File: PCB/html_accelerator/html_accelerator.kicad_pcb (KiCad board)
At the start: 4 copper layers, 129.3 x 104.4 mm, 170 parts, among them J1 Bus_PCI_Express_x16, J2 PCIexpress_bracket, U1 MCS9990, U10 AU6438BS, U11 EMMC_4G, U12 MCS9990, U2 AP1513, U3 CAT24C256YI-GT3, U4 AU6438BS, U5 EMMC_4G, U6 EMMC_4G, U7 EMMC_4G, U8 AU6438BS, U9 AU6438BS, Y1 12MHz, Y2 12MHz, Y3 12MHz, Y4 12MHz, Y5 12MHz

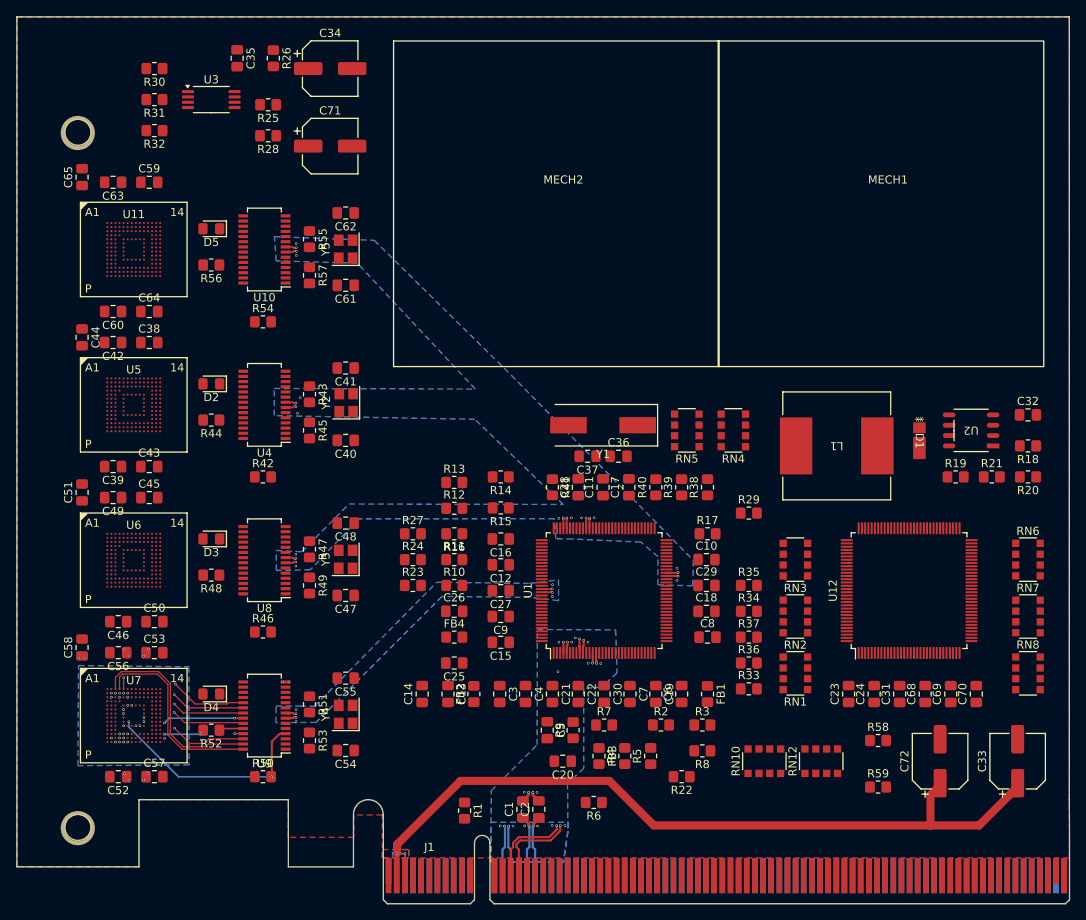
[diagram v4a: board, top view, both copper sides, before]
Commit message: highspeed routing + EMMC routing #1
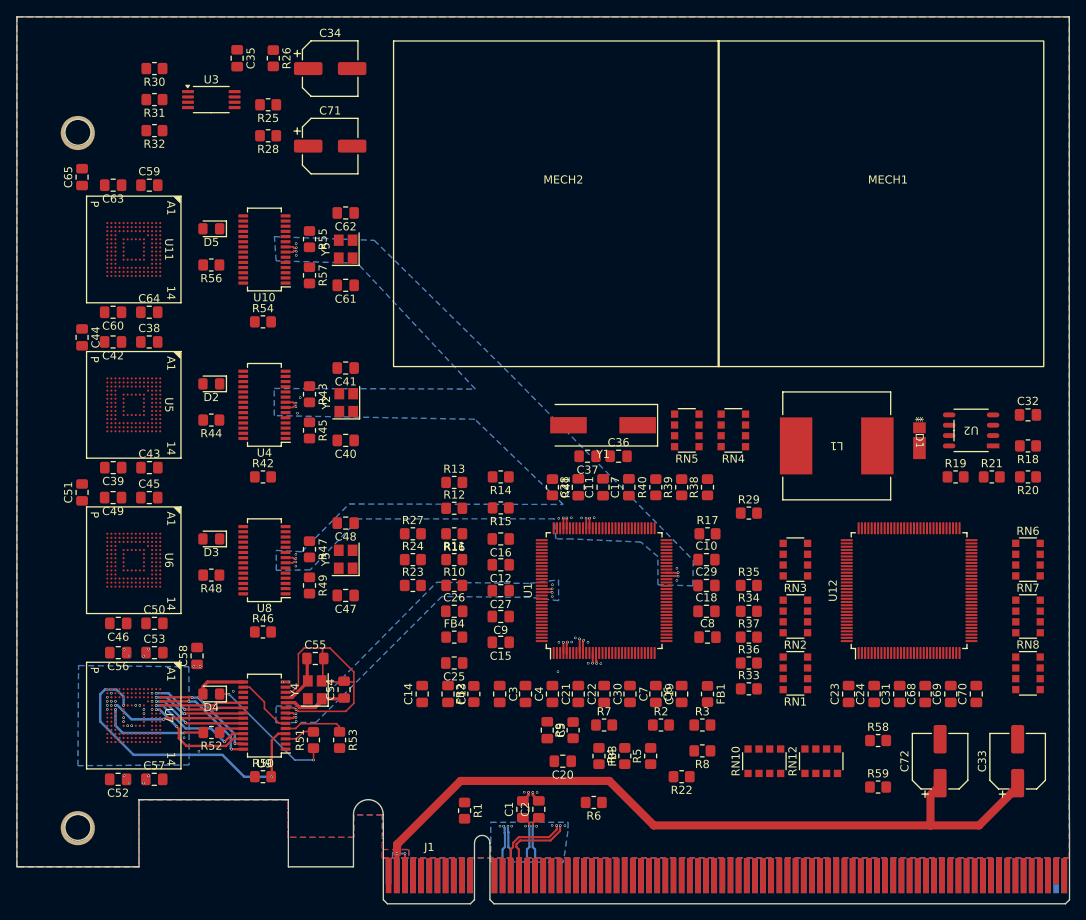
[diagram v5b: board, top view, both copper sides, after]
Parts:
- moved C58 14.2 mm to (136.4, 129.1)
- moved C54 7.49 mm to (154.5, 133.3), turned to 90 degrees
- moved Y4 4.85 mm to (150.9, 133.3)
- moved C55 4.44 mm to (151.0, 129.4), turned to 0 degrees
- moved R51 4.41 mm to (150.8, 139.4), turned to 90 degrees
- moved R53 3.70 mm to (154.0, 139.4)
- moved C59 0.36 mm to (130.6, 71.3)
- moved C63 0.36 mm to (126.1, 71.3)
- moved C57 0.32 mm to (131.2, 144.3)
- moved C52 0.32 mm to (126.8, 144.3)
- moved R52 0.29 mm to (138.2, 138.5)
- moved C46 0.21 mm to (126.8, 125.1)
- moved C50 0.21 mm to (131.2, 125.1)
- moved C39 0.13 mm to (126.2, 106.0)
- moved C43 0.13 mm to (130.6, 106.0)
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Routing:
- net GND: track 0.02 -> 35.1 mm, vias 42 -> 43
- net USB2_LED: track 0.00 -> 16.3 mm, vias 0 -> 2
- net /eMMC3/DATA_0: track 25.0 -> 13.1 mm, vias 0 -> 2
- net /eMMC3/DATA_1: track 24.3 -> 13.5 mm, vias 0 -> 2
- net Net-(U7A-RST_N): track 28.1 -> 38.3 mm, vias 3 -> 2
- net Net-(U9-XTAL_IN): track 0.00 -> 8.37 mm
- net Net-(U9-EXT_R): track 0.00 -> 7.80 mm
- net Net-(U9-V3.3_PHY_IN): track 0.00 -> 7.57 mm
- net /eMMC3/DATA_2: track 17.5 -> 10.4 mm, vias 2 -> 0
- net Net-(U9-XTAL_OUT): track 0.00 -> 6.74 mm
- net /eMMC3/DATA_3: track 18.2 -> 11.5 mm
- net +5V: track 0.00 -> 6.18 mm
- net /eMMC3/DATA_4: track 17.7 -> 11.6 mm
- net /eMMC3/DATA_5: track 17.4 -> 11.8 mm
- net /eMMC3/DATA_6: track 17.2 -> 13.0 mm
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- added copper zone on In2.Cu, net GND
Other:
- board text removed: "ToDo: Route EMMC at 50ohm single end with shield"
- board text removed: "ToDo: update 85 rounting with new cleaner rules"

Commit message: EMMC wiring checkpoint
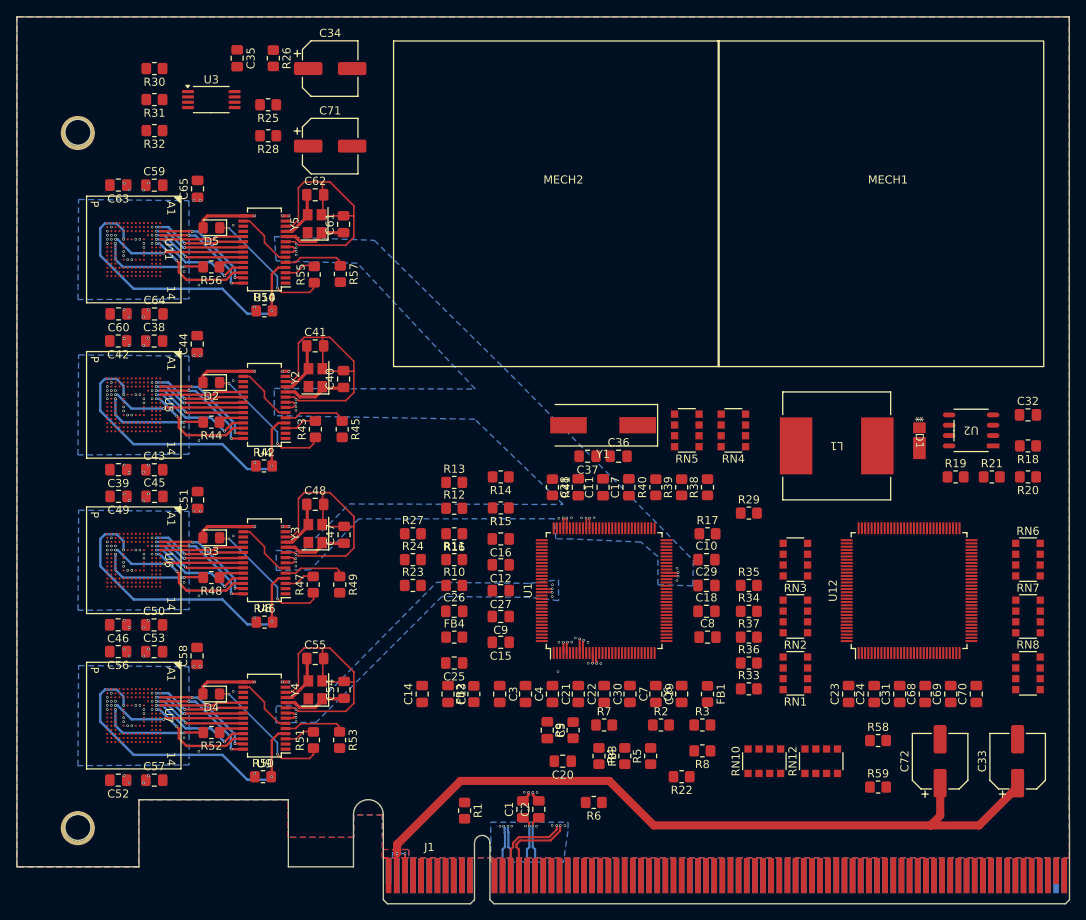
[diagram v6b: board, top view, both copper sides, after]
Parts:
- moved C65 14.3 mm to (136.5, 71.7)
- moved C51 14.2 mm to (136.5, 110.0)
- moved C44 14.2 mm to (136.5, 90.8), turned to 90 degrees
- moved C40 7.54 mm to (154.4, 95.1), turned to 90 degrees
- moved C61 7.51 mm to (154.4, 76.1), turned to 90 degrees
- moved C47 7.46 mm to (154.5, 114.2), turned to 90 degrees
- moved Y5 4.93 mm to (150.9, 76.0)
- moved Y3 4.89 mm to (151.0, 114.1)
- moved Y2 4.87 mm to (151.0, 94.9)
- moved C41 4.63 mm to (151.0, 91.0), turned to 0 degrees
- moved C48 4.39 mm to (151.0, 110.5), turned to 0 degrees
- moved R55 4.39 mm to (150.8, 82.3), turned to 90 degrees
- moved R47 4.36 mm to (150.7, 120.4), turned to 90 degrees
- moved R43 4.36 mm to (151.0, 101.3), turned to 90 degrees
- moved C62 4.35 mm to (151.0, 72.5), turned to 0 degrees
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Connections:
- C41 pad 2: GND -> Net-(U4-XTAL_OUT)
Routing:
- net GND: track 35.1 -> 140.3 mm, vias 43 -> 79
- net +5V: track 6.18 -> 75.2 mm, vias 0 -> 8
- net Net-(U10-#CHIP_RST): track 0.00 -> 38.6 mm, vias 0 -> 2
- net Net-(U6A-RST_N): track 0.00 -> 38.6 mm, vias 0 -> 2
- net Net-(U4-#CHIP_RST): track 0.00 -> 38.6 mm, vias 0 -> 2
- net /eMMC2/VDD_3v3_EMMC2: track 0.00 -> 24.9 mm, vias 0 -> 19
- net /eMMC1/VDD_3v3_EMMC1: track 0.00 -> 24.9 mm, vias 0 -> 19
- net /eMMC4/VDD_3v3_EMMC4: track 0.00 -> 24.9 mm, vias 0 -> 19
- net USB0_LED: track 0.00 -> 16.6 mm, vias 0 -> 2
- net USB3_LED: track 0.00 -> 16.6 mm, vias 0 -> 2
- net USB1_LED: track 0.00 -> 16.6 mm, vias 0 -> 2
- net Net-(U4-SDCMD): track 0.00 -> 16.5 mm, vias 0 -> 2
- net Net-(U10-SDCMD): track 0.00 -> 16.5 mm, vias 0 -> 2
- net Net-(U6A-CMD): track 0.00 -> 16.5 mm, vias 0 -> 2
- net /eMMC2/DATA_7: track 0.00 -> 13.6 mm, vias 0 -> 2
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- added copper zone on In1.Cu, net /eMMC1/VDD_3v3_EMMC1
- added copper zone on In1.Cu, net /eMMC2/VDD_3v3_EMMC2
- added copper zone on In1.Cu, net /eMMC4/VDD_3v3_EMMC4
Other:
- rule pad_to_mask_clearance: 0.04 -> 0.02
